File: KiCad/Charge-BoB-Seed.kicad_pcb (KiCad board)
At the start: 2 copper layers, 10 parts, among them J1 Screw_01x10, J10 Screw_01x10, J2 Screw_01x10, J3 Pin, J4 Socket, J5 Socket, J6 Socket, J7 Socket, J8 Pin, J9 Screw_01x10

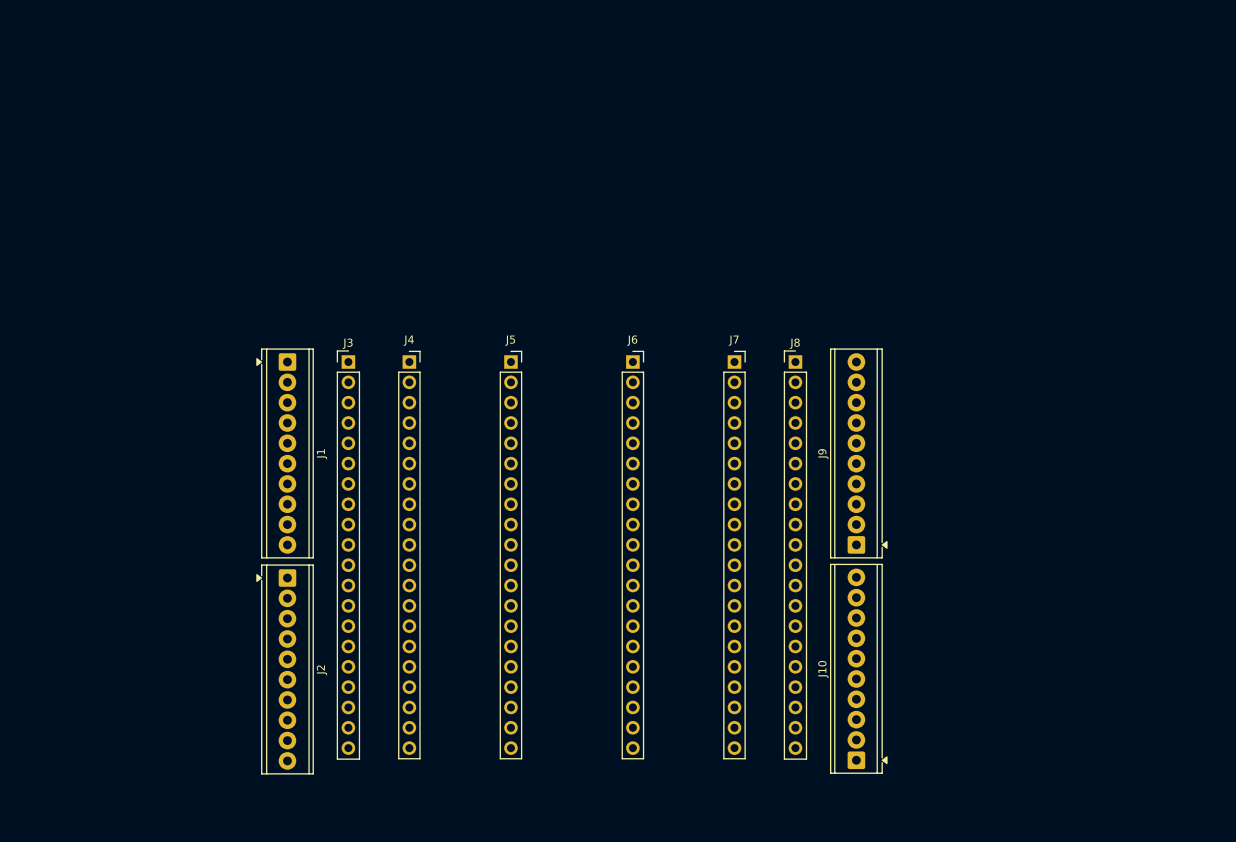
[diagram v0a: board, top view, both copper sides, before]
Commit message: Added Reference Image in KiCad to be used as Silkscreen on PCB
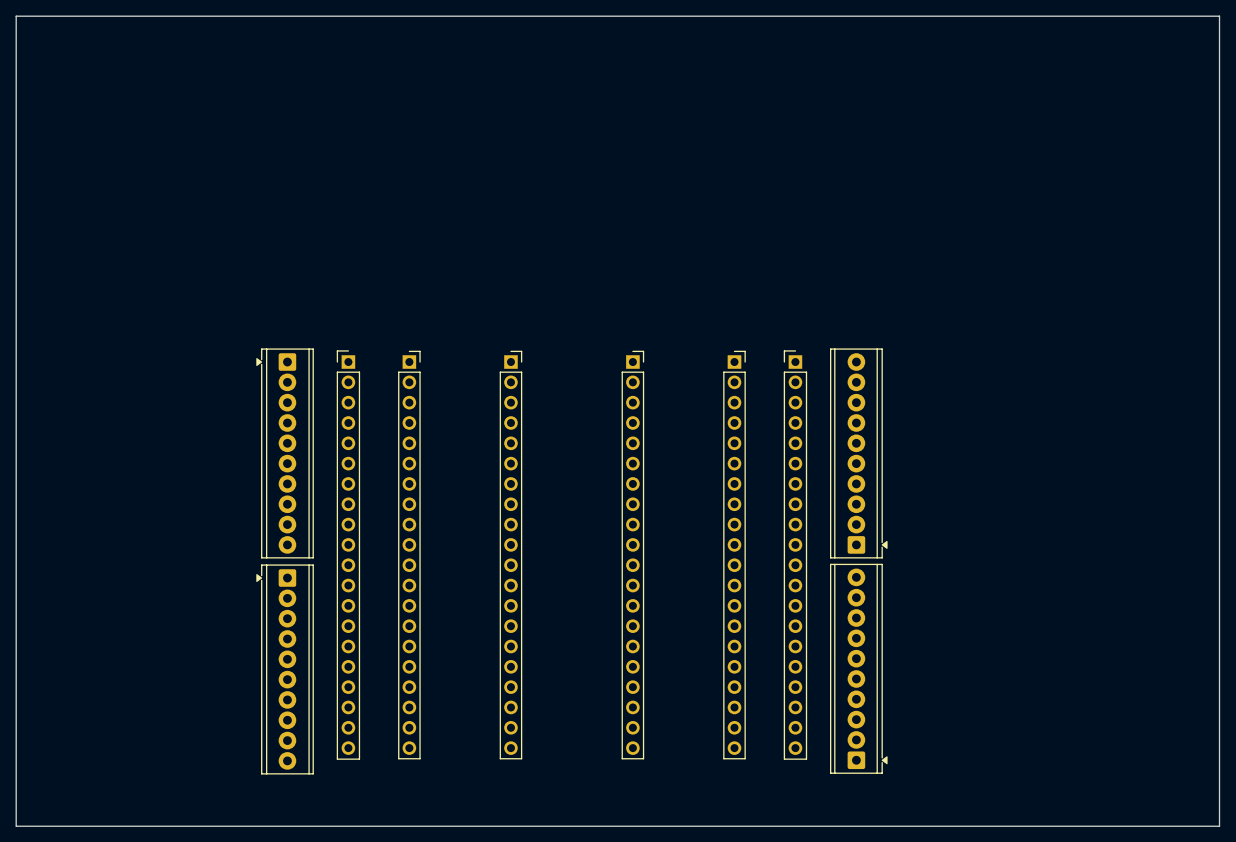
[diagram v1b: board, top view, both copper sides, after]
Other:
- board outline added: 150.4 x 101.3 mm
